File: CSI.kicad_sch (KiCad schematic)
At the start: 0 parts

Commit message: [#82054] Rebase CSI branch
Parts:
- added C100 (x2), C101 (x2), C104, C105, C93, C98, C99: C_100n_0402, antmicro-footprints:C_0402_1005Metric, symbol antmicroCapacitors0402:C_100n_0402
- added C102, C103, C98, C99: C_1u_0402, antmicro-footprints:C_0402_1005Metric, symbol antmicroCapacitors0402:C_1u_0402
- added D18, D20, D24, D25: LED_G_0603_LTST-C190GKT, antmicro-footprints:LED_0603_1608Metric_G, symbol antmicroLEDIndicationDiscrete:LED_G_0603_LTST-C190GKT
- added J7, J8: Conn_FFC_WE_68715014522, antmicro-footprints:Conn_FFC_WE_68715014x22, symbol antmicroFCCConnectors:Conn_FFC_WE_68715014522
- added R109, R111: R_4x2k2_0201_array, antmicro-footprints:R_Array_4x0201_Panasonic_EXB18V, symbol antmicroResistorNetworksArrays:R_4x2k2_0201_array
- added R110, R180: R_100k_0402, antmicro-footprints:R_0402_1005Metric, symbol antmicroResistors0402:R_100k_0402
- added R112, R120, R163, R193, R194: R_10k_0402, antmicro-footprints:R_0402_1005Metric, symbol antmicroResistors0402:R_10k_0402
- added R113, R114, R121, R122: R_4k7_0402, antmicro-footprints:R_0402_1005Metric, symbol antmicroResistors0402:R_4k7_0402
- added R123, R125: R_4x0R_0201_array, antmicro-footprints:R_Array_4x0201_Panasonic_EXB18V, symbol antmicroResistorNetworksArrays:R_4x0R_0201_array
- added R124, R132: R_200R_0402, antmicro-footprints:R_0402_1005Metric, symbol antmicroResistors0402:R_200R_0402
- added R161, R162, R166, R167, R168, R171, R174, R179: R_0R_0402, antmicro-footprints:R_0402_1005Metric, symbol antmicroResistors0402:R_0R_0402
- added R197, R206: R_470R_0402, antmicro-footprints:R_0402_1005Metric, symbol antmicroResistors0402:R_470R_0402
- added TP36, TP37, TP38, TP39, TP40, TP41, TP42, TP43: TP_0.75mm_SMD, antmicro-footprints:TP_SMD_0.75mm, symbol antmicroTestPoints:TP_0.75mm_SMD
- added U24, U25, U27, U28: AP22615A_TSOT26, antmicro-footprints:TSOT23-6, symbol antmicroPMICPowerDistributionSwitchesLoadDrivers:AP22615A_TSOT26
- added U26: PI4MSD5V9548AZDEX, antmicro-footprints:VQFN-24-1EP_3.8x3.8x1.0mm_P0.5mm, symbol antmicroLogicSignalSwitchesMultiplexersDecoders:PI4MSD5V9548AZDEX
- added U31, U32: NTS0102_XSON, antmicro-footprints:XSON-8_1x1.95mm_P0.5mm, symbol antmicroLogicTranslatorsLevelShifters:NTS0102_XSON
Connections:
- new net: J8.39, R125.8 (R1.2)
- new net: J8.40, R125.7 (R2.2)
- new net: J8.41, R125.6 (R3.2)
- new net: J8.42, R125.5 (R4.2)
- new net: D20.2 (A), R197.1
- new net: D25.2 (A), R206.1
- new net: D24.2 (A), R124.1
- new net: D18.2 (A), R132.1
- new net: J7.42, R123.5 (R4.2)
- new net: J7.41, R123.6 (R3.2)
- new net: J7.40, R123.7 (R2.2)
- new net: J7.39, R123.8 (R1.2)
- new net +1V8: C104.2, C105.2, C93.2, R163.1, R167.2, R171.2, R179.2, U26.21 (VCC), U31.3 (VCC_{A}), U31.6 (OE), U32.3 (VCC_{A}), U32.6 (OE)
- new net +3V3: C100.2, C101.1, C101.2, C99.1, R112.1, R120.1, R166.2, R174.2, R193.2, R194.2, U25.6 (IN), U28.6 (IN), U31.7 (VCC_{B}), U32.7 (VCC_{B})
- new net +5V: C100.1, C98.1, U24.6 (IN), U27.6 (IN)
- new net CSI0.CLK+: J7.11
- new net CSI0.CLK-: J7.10
- new net CSI0.D0+: J7.8
- new net CSI0.D0-: J7.7
- new net CSI0.D1+: J7.6
- new net CSI0.D1-: J7.5
- new net CSI0.D2+: J7.4
- new net CSI0.D2-: J7.3
- new net CSI0.D3+: J7.2
- new net CSI0.D3-: J7.1
- new net CSI1.CLK+: J7.29
- new net CSI1.CLK-: J7.28
- new net CSI1.D0+: J7.26
- new net CSI1.D0-: J7.25
- new net CSI1.D1+: J7.24
- new net CSI1.D1-: J7.23
- new net CSI1.D2+: J7.22
- new net CSI1.D2-: J7.21
- new net CSI1.D3+: J7.20
- new net CSI1.D3-: J7.19
- new net CSI2.CLK+: J8.11
- new net CSI2.CLK-: J8.10
- new net CSI2.D0+: J8.8
- new net CSI2.D0-: J8.7
- new net CSI2.D1+: J8.6
- new net CSI2.D1-: J8.5
- new net CSI2.D2+: J8.4
- new net CSI2.D2-: J8.3
- new net CSI2.D3+: J8.2
- new net CSI2.D3-: J8.1
- new net CSI3.CLK+: J8.29
- new net CSI3.CLK-: J8.28
- new net CSI3.D0+: J8.26
- new net CSI3.D0-: J8.25
- new net CSI3.D1+: J8.24
- new net CSI3.D1-: J8.23
- new net CSI3.D2+: J8.22
- new net CSI3.D2-: J8.21
- new net CSI3.D3+: J8.20
- new net CSI3.D3-: J8.19
- new net CSIA_3V3: C102.2, J7.47, J7.48, R132.2, U25.1 (OUT)
- new net CSIA_3V3_ISET: R114.2, U25.5 (ISET)
- new net CSIA_5V: C103.2, J7.49, J7.50, R197.2, U24.1 (OUT)
- new net CSIA_5V_ISET: R113.2, U24.5 (ISET)
- new net CSIA_FLG: R112.2, R120.2, U24.3 (FLG), U25.3 (FLG), U27.3 (FLG), U28.3 (FLG)
- new net CSIA_I2C_VCC: R109.5 (R4.2), R109.6 (R3.2), R109.7 (R2.2), R109.8 (R1.2), R166.1, R171.1
- new net CSIA_PEN: R110.2, R180.2, R193.1, R194.1, U24.4 (EN), U25.4 (EN), U27.4 (EN), U28.4 (EN)
- new net CSIB_3V3: C98.2, J8.47, J8.48, R124.2, U28.1 (OUT)
- new net CSIB_3V3_ISET: R122.2, U28.5 (ISET)
- new net CSIB_5V: C99.2, J8.49, J8.50, R206.2, U27.1 (OUT)
- new net CSIB_5V_ISET: R121.2, U27.5 (ISET)
- new net CSIB_I2C_VCC: R111.5 (R4.2), R111.6 (R3.2), R111.7 (R2.2), R111.8 (R1.2), R174.1, R179.1
- new net GND: C100.1, C100.2, C101.1, C101.2, C102.1, C103.1, C104.1, C105.1, C93.1, C98.1, C98.2, C99.1, C99.2, D18.1 (C), D20.1 (C), D24.1 (C), D25.1 (C), J7.12, J7.15, J7.18, J7.27, J7.30, J7.9, J7.MP1 (MP), J7.MP2 (MP), J8.12, J8.15, J8.18, J8.27, J8.30, J8.9, J8.MP1 (MP), J8.MP2 (MP), R110.1, R113.1, R114.1, R121.1, R122.1, R168.1, R180.1, U24.2 (GND), U25.2 (GND), U26.18 (A2), U26.23 (A1), U26.9 (GND), U27.2 (GND), U28.2 (GND), U31.2 (GND), U32.2 (GND)
- new net I2C_MUX_A0: R167.1, R168.2, U26.22 (A0)
- new net I2C_MUX_RESET: R163.2, U26.24 (~{RESET})
- new net I2C_MUX_SCL: R162.1, U26.19 (SCL)
- new net I2C_MUX_SDA: R161.1, U26.20 (SDA)
- new net I2C_{CAM}.SCL: R162.2
- new net I2C_{CAM}.SDA: R161.2
- new net MUX_I2C_4_SCL: TP37.1, U26.11 (SC4)
- new net MUX_I2C_4_SDA: TP36.1, U26.10 (SD4)
- new net MUX_I2C_5_SCL: TP39.1, U26.13 (SC5)
- new net MUX_I2C_5_SDA: TP38.1, U26.12 (SD5)
- new net MUX_I2C_6_SCL: TP41.1, U26.15 (SC6)
- new net MUX_I2C_6_SDA: TP40.1, U26.14 (SD6)
- new net MUX_I2C_7_SCL: TP43.1, U26.17 (SC7)
- new net MUX_I2C_7_SDA: TP42.1, U26.16 (SD7)
- new net SCL_CAM0: R109.3 (R3.1), R123.2 (R2.1), U26.2 (SC0)
- new net SCL_CAM1: R109.1 (R1.1), R123.4 (R4.1), U26.4 (SC1)
- new net SCL_CAM2: R111.3 (R3.1), R125.2 (R2.1), U26.6 (SC2)
- new net SCL_CAM3: R111.1 (R1.1), R125.4 (R4.1), U26.8 (SC3)
- new net SDA_CAM0: R109.4 (R4.1), R123.1 (R1.1), U26.1 (SD0)
- new net SDA_CAM1: R109.2 (R2.1), R123.3 (R3.1), U26.3 (SD1)
- new net SDA_CAM2: R111.4 (R4.1), R125.1 (R1.1), U26.5 (SD2)
- new net SDA_CAM3: R111.2 (R2.1), R125.3 (R3.1), U26.7 (SD3)
- new net VSYNC_CAM0: U31.5 (A_{1})
- new net VSYNC_CAM0_3V3: J7.32, U31.8 (B_{1})
- new net VSYNC_CAM1: U31.4 (A_{2})
- new net VSYNC_CAM1_3V3: J7.34, U31.1 (B_{2})
- new net VSYNC_CAM2: U32.5 (A_{1})
- new net VSYNC_CAM2_3V3: J8.32, U32.8 (B_{1})
- new net VSYNC_CAM3: U32.4 (A_{2})
- new net VSYNC_CAM3_3V3: J8.34, U32.1 (B_{2})
- no-connect marks 0 -> 29
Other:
- note added: "ALL SWITCHES 1.5A CURRENT LIMIT"
- note added: "CSI connector"
- note added: "CSI0 x2"
- note added: "CSI0 x4"
- note added: "CSI1 x2"
- note added: "CSI1 x4"
- note added: "CSI2 x2"
- note added: "CSI2 x4"
- note added: "I2C Mux"
- note added: "Jetson AGX Orin doesn't have vsync and hsync pins but I connected them to the GPIO just in case"
- note added: "Level shifters"
- note added: "Power switches"
- note added: "Route to GPIO: CSIA_PEN CSIB_PEN CSIA_FLG CSIB_FLG VSYNC_CAM0 VSYNC_CAM1 VSYNC_CAM2 VSYNC_CAM3 Veryfy GPIO voltages before connection vsync level shifters might be unnecesairy"

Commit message: [#81970] Route traces from root schematic on other schematics
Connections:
- net CSIA_FLG renamed CAM_CTRL.CSIA_FLG
- net CAM_CTRL.CSIA_FLG: no longer R120.2, U27.3 (FLG), U28.3 (FLG)
- net CSIA_PEN renamed CAM_CTRL.CSIA_PEN
- net CAM_CTRL.CSIA_PEN: no longer R180.2, R194.1, U27.4 (EN), U28.4 (EN)
- net VSYNC_CAM0 renamed CAM_CTRL.VSYNC_CAM0
- net VSYNC_CAM1 renamed CAM_CTRL.VSYNC_CAM1
- net VSYNC_CAM2 renamed CAM_CTRL.VSYNC_CAM2
- net VSYNC_CAM3 renamed CAM_CTRL.VSYNC_CAM3
- new net CAM_CTRL.CSIB_FLG: R120.2, U27.3 (FLG), U28.3 (FLG)
- new net CAM_CTRL.CSIB_PEN: R180.2, R194.1, U27.4 (EN), U28.4 (EN)
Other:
- note added: "EN input logic high 1.2V"
- note added: "GPIO 1V8, 3V3 tolerant"
- note removed: "Route to GPIO: CSIA_PEN CSIB_PEN CSIA_FLG CSIB_FLG VSYNC_CAM0 VSYNC_CAM1 VSYNC_CAM2 VSYNC_CAM3 Veryfy GPIO voltages before connection vsync level shifters might be unnecesairy"
- moved on the sheet: C100, C101, C105, C98, C99, R110, R112, R113, R114, R120, R121, R122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

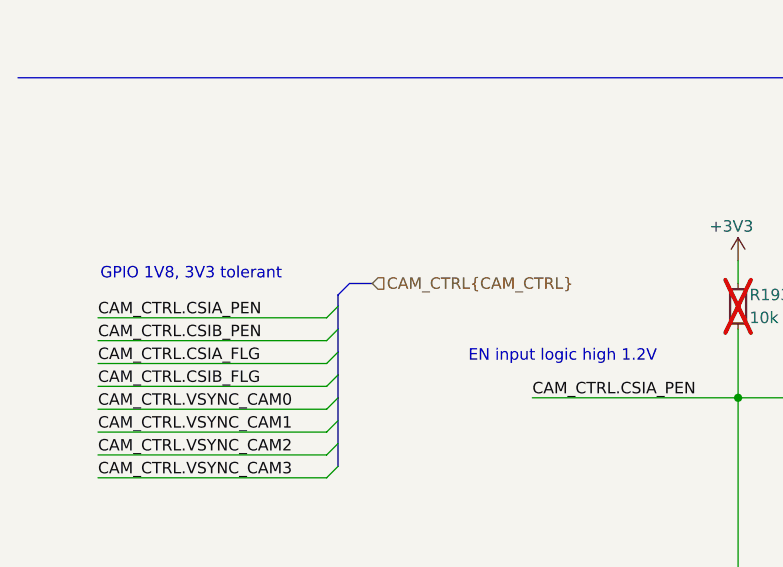
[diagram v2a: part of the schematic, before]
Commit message: [#81970] Route present on root GPIO pins on CSI and Peripherals sheets
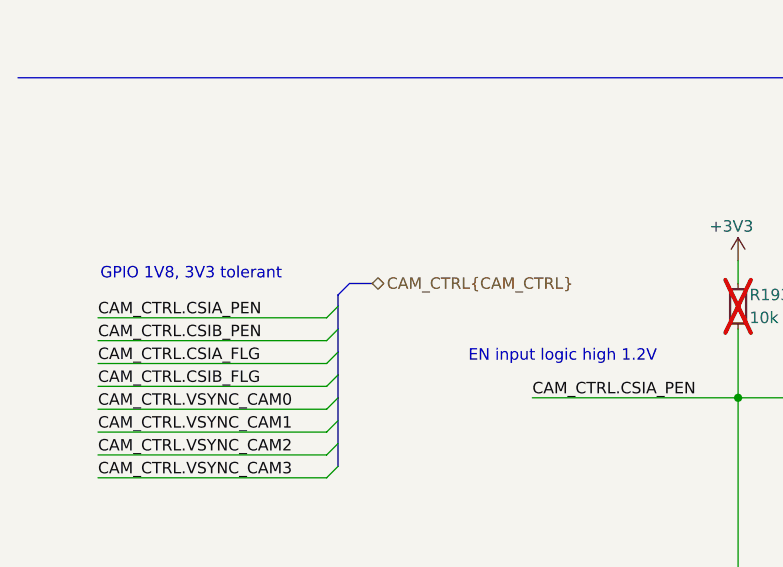
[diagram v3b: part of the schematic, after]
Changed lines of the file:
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@@
 	)
 	(hierarchical_label "CAM_CTRL{CAM_CTRL}"
-		(shape input)
+		(shape bidirectional)
 		(at 52.07 203.2 0)
 		(effects

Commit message: [#82757] Rename project to jetson-agx-thor-baseboard
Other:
- title: Jetson Orin AGX Baseboard -> Jetson AGX Thor Baseboard
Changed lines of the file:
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@@
 	(paper "A3")
 	(title_block
-		(title "Jetson Orin AGX Baseboard")
+		(title "Jetson AGX Thor Baseboard")
 		(date "2025-08-11")
 		(rev "1.0.0")

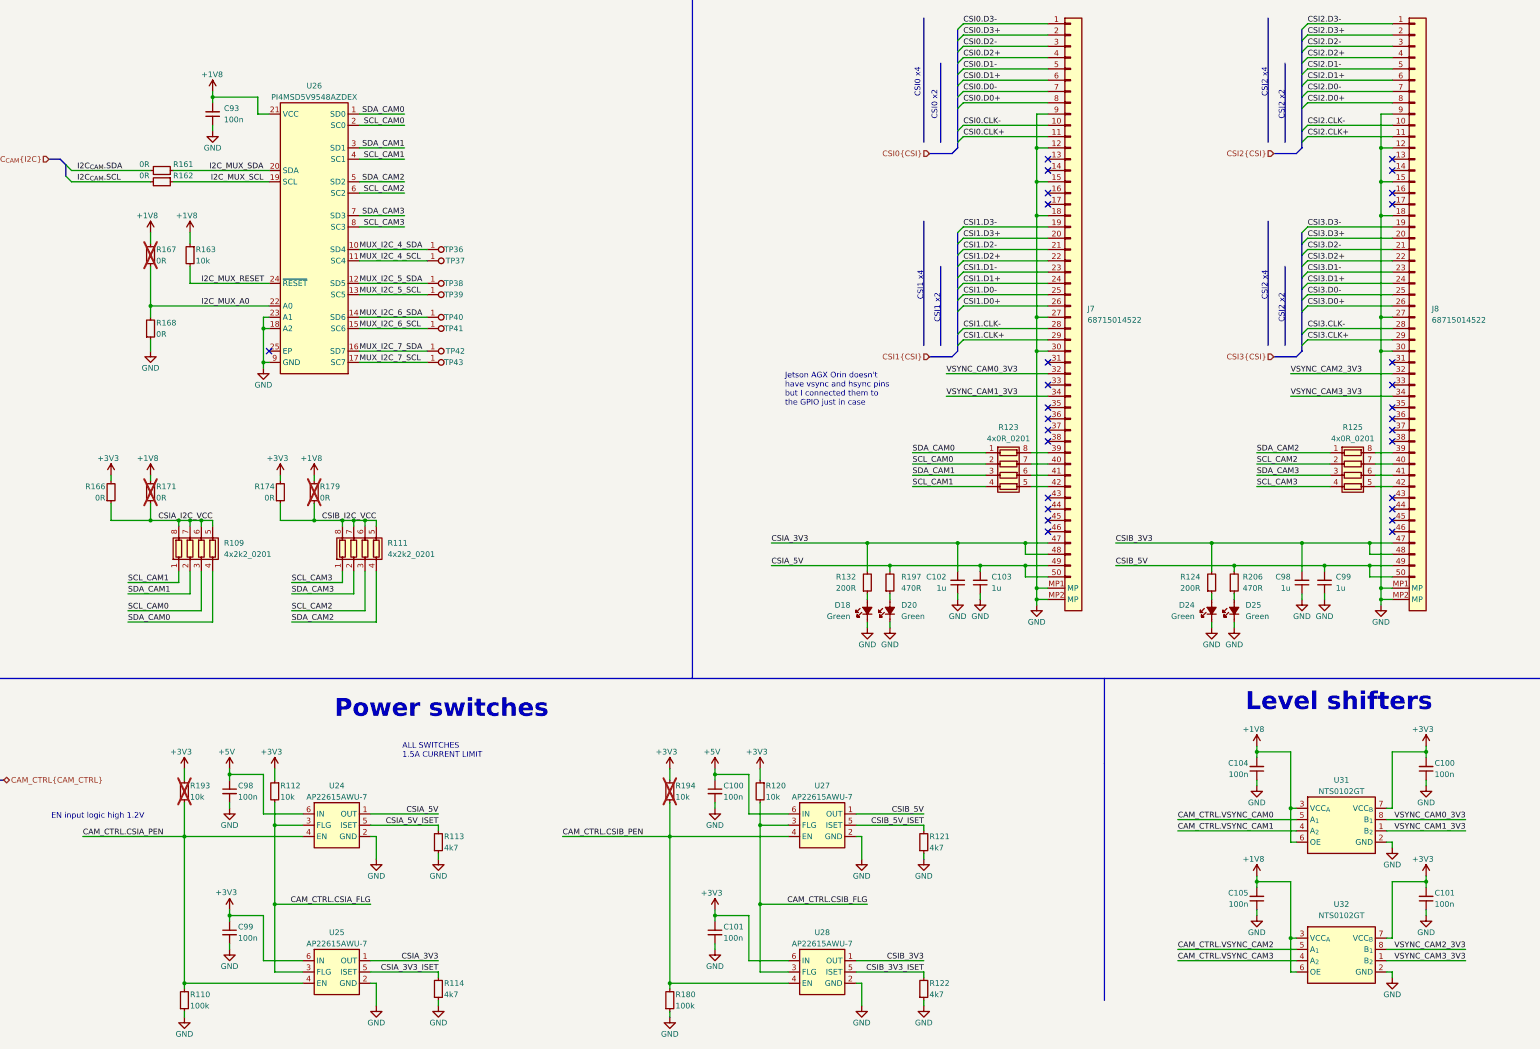
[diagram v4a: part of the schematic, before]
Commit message: [#82757] Cleanup: reorganise page numbers and fix annotations
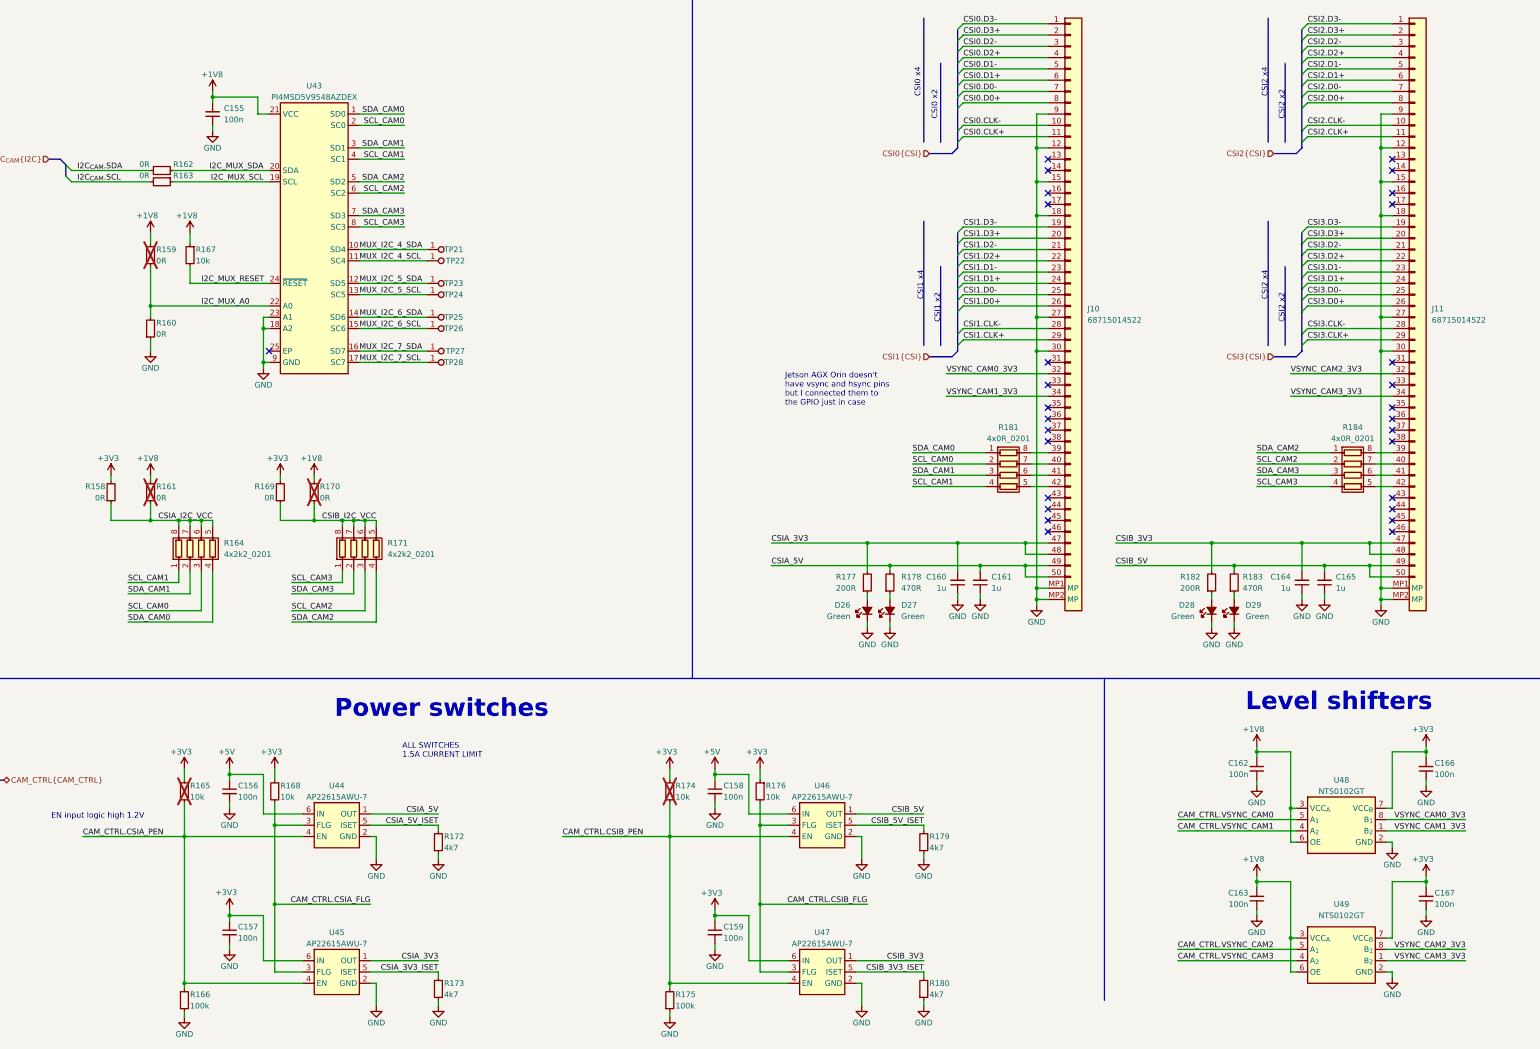
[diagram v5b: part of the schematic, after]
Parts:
- renumbered C93 to C155, C98 to C156, C99 to C157, C100 to C158, C101 to C159, C102 to C160, C103 to C161, C104 to C162, C105 to C163, C98 to C164, C99 to C165, C100 to C166, C101 to C167, D18 to D26, D20 to D27, D24 to D28, D25 to D29, J7 to J10, J8 to J11, R166 to R158, R167 to R159, R168 to R160, R171 to R161, R161 to R162, R162 to R163, R109 to R164, R193 to R165, R110 to R166, R163 to R167, R112 to R168, R174 to R169, R179 to R170, R111 to R171, R113 to R172, R114 to R173, R194 to R174, R180 to R175, R120 to R176, R132 to R177, R197 to R178, R121 to R179, R122 to R180, R123 to R181, R124 to R182, R206 to R183, R125 to R184, TP36 to TP21, TP37 to TP22, TP38 to TP23, TP39 to TP24, TP40 to TP25, TP41 to TP26, TP42 to TP27, TP43 to TP28, U26 to U43, U24 to U44, U25 to U45, U27 to U46, U28 to U47, U31 to U48, U32 to U49
